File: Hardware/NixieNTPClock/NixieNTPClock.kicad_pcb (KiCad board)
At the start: 2 copper layers, 58 parts, among them J1 Conn_01x02_Male, Q1 BC850, Q2 Q_NMOS_GDS, Q3 FQT4N25TF, Q4 FQT4N25TF, Q5 FQT4N25TF, Q6 FQT4N25TF, U1 74HC7014, U10 DS18B20, U11 ESP32-nodeMCU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

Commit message: Continu on PCB ...
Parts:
- U3: footprint Housings_DIP:DIP-16_W7.62mm_Socket -> Package_DIP:DIP-16_W7.62mm_Socket_LongPads
- moved U10 193.5 mm to (238.8, 118.4), turned to 180 degrees
- moved C13 181.6 mm to (230.4, 118.6), turned to 90 degrees
- moved R14 158.8 mm to (234.2, 113.8), turned to 180 degrees
- moved C14 150.5 mm to (204.2, 107.7), turned to 90 degrees
- moved C15 137.0 mm to (198.1, 107.7), turned to 90 degrees
- moved U2 130.9 mm to (77.7, 87.1)
- moved Q4 118.9 mm to (140.7, 75.2), turned to 180 degrees
- moved Q1 109.1 mm to (87.1, 93.8), turned to 90 degrees
- moved RV1 107.9 mm to (90.7, 100.7)
- moved Q6 106.2 mm to (197.7, 75.2), turned to 180 degrees
- moved R16 106.0 mm to (205.2, 75.2), turned to 90 degrees
- moved C1 103.6 mm to (71.0, 97.3), turned to 180 degrees
- moved R2 94.5 mm to (87.1, 86.9), turned to 270 degrees
- moved R13 91.7 mm to (148.6, 75.2), turned to 90 degrees
- moved R15 87.2 mm to (156.2, 75.2), turned to 270 degrees
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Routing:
- net Net-(TP1-Pad1): track 0.00 -> 105.6 mm
- net Net-(R8-Pad1): track 0.00 -> 28.7 mm
- net Net-(U1-Pad2): track 0.00 -> 28.2 mm
- net GND: track 0.00 -> 27.9 mm
- net /5: track 112.0 -> 85.8 mm, vias 1 -> 0
- net +5V: track 0.00 -> 20.8 mm
- net TEMP: track 0.00 -> 20.8 mm
- net Net-(U1-Pad6): track 0.00 -> 17.8 mm
- net Net-(U1-Pad4): track 0.00 -> 17.7 mm
- net Net-(Q6-Pad2): track 0.00 -> 11.8 mm
- net Net-(Q3-Pad2): track 0.00 -> 11.8 mm
- net Net-(Q5-Pad2): track 0.00 -> 11.4 mm
- net Net-(Q4-Pad2): track 0.00 -> 11.3 mm
- net +3V3: track 0.00 -> 8.13 mm
- net P_UNIT_H: track 0.00 -> 4.84 mm
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
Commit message: Hardware: power supply
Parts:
- moved L2 121.4 mm to (106.0, 106.4)
- moved U9 116.3 mm to (99.1, 101.9), turned to 270 degrees
- moved R11 103.7 mm to (92.2, 111.3)
- moved C11 101.9 mm to (108.2, 115.3), turned to 270 degrees
- moved C9 93.9 mm to (92.4, 94.2), turned to 180 degrees
- moved C12 85.1 mm to (100.3, 115.3), turned to 270 degrees
- moved R10 85.0 mm to (92.2, 115.1), turned to 180 degrees
- moved L1 82.6 mm to (69.8, 55.1), turned to 90 degrees
- moved D1 79.0 mm to (80.3, 65.9), turned to 90 degrees
- moved R9 75.8 mm to (92.7, 102.6), turned to 90 degrees
- moved C10 71.8 mm to (100.3, 106.9), turned to 270 degrees
- moved R17 55.8 mm to (32.8, -2.79), turned to 180 degrees
- moved C6 52.4 mm to (91.2, 66.0)
- moved D2 45.8 mm to (31.2, 2.03)
- moved R7 44.8 mm to (90.5, 77.5)
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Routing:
- net +12V: track 0.00 -> 70.9 mm, vias 0 -> 2
- net +5V: track 20.8 -> 43.0 mm
- net Net-(R10-Pad2): track 0.00 -> 19.3 mm
- net Net-(C2-Pad1): track 0.00 -> 18.6 mm
- net Net-(C10-Pad2): track 0.00 -> 17.3 mm
- net Net-(C8-Pad1): track 0.00 -> 15.7 mm
- net Net-(D1-Pad2): track 0.00 -> 13.9 mm
- net Net-(R1-Pad2): track 0.00 -> 11.6 mm
- net Net-(R9-Pad1): track 0.00 -> 8.49 mm
- net Net-(Q2-Pad1): track 0.00 -> 6.15 mm
- net Net-(R6-Pad2): track 0.00 -> 4.12 mm
- net Net-(R7-Pad1): track 0.00 -> 3.98 mm
- net GND: track 27.9 -> 31.7 mm
- net Net-(C5-Pad2): track 0.00 -> 3.30 mm
- net Net-(C10-Pad1): track 0.00 -> 2.84 mm

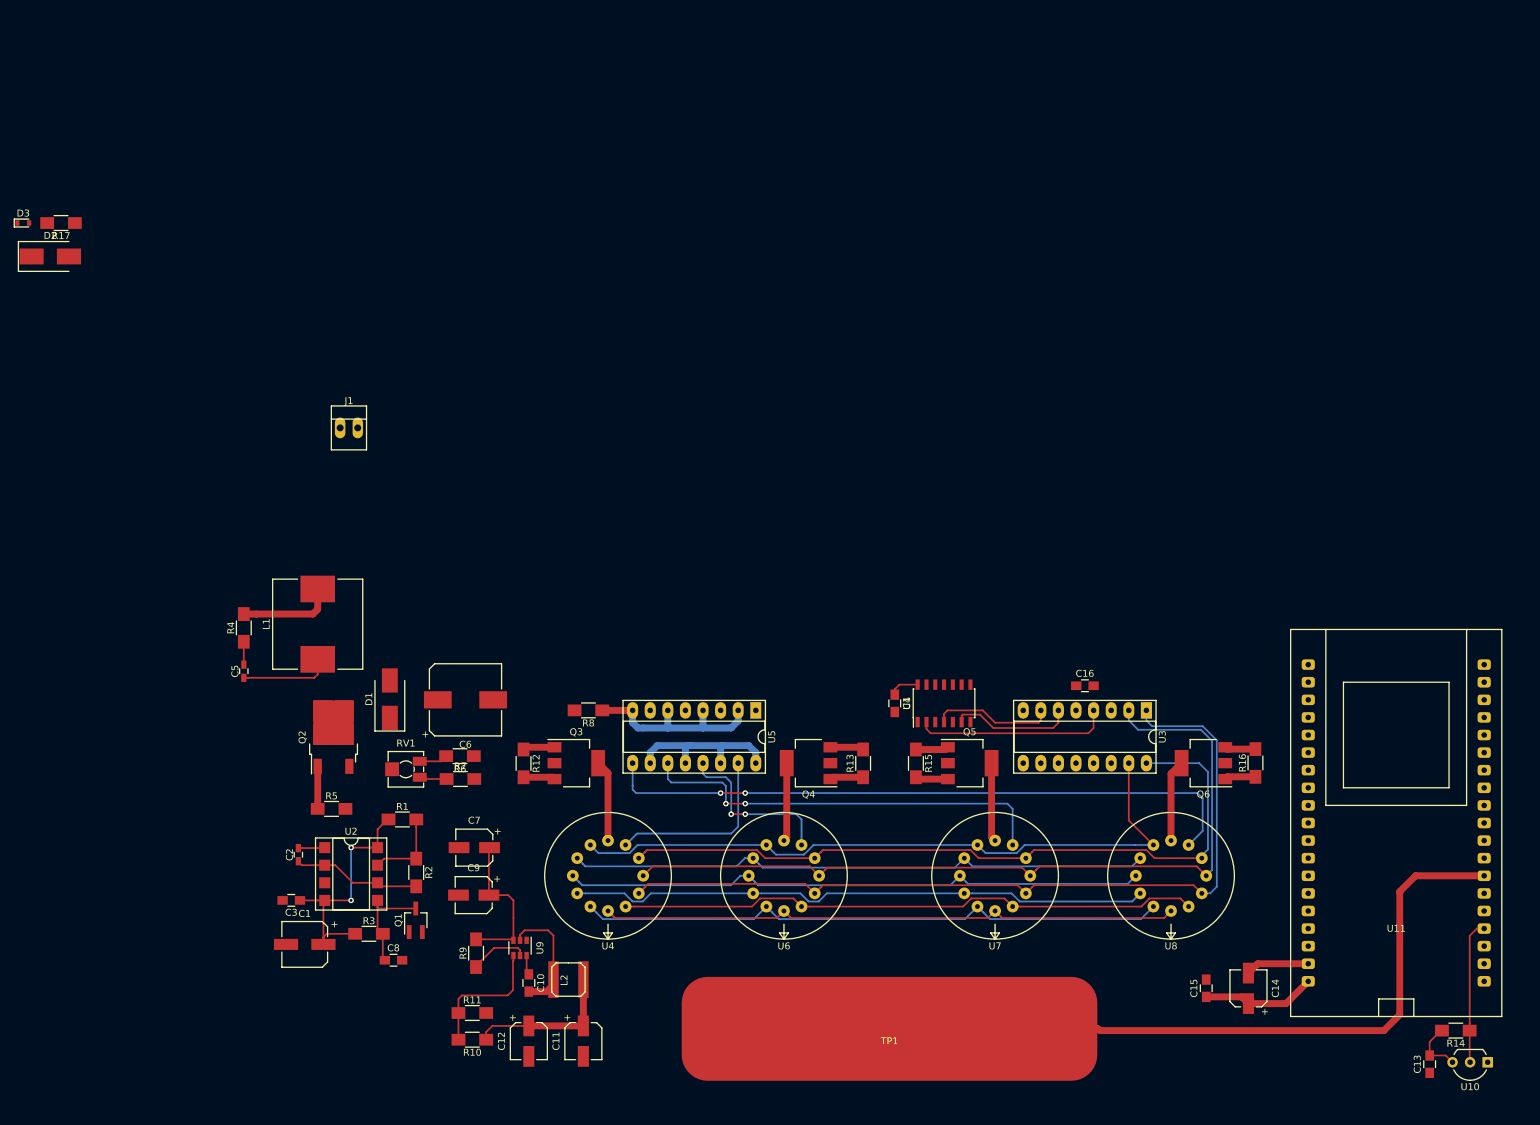
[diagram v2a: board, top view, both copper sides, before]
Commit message: Continuous routing ...
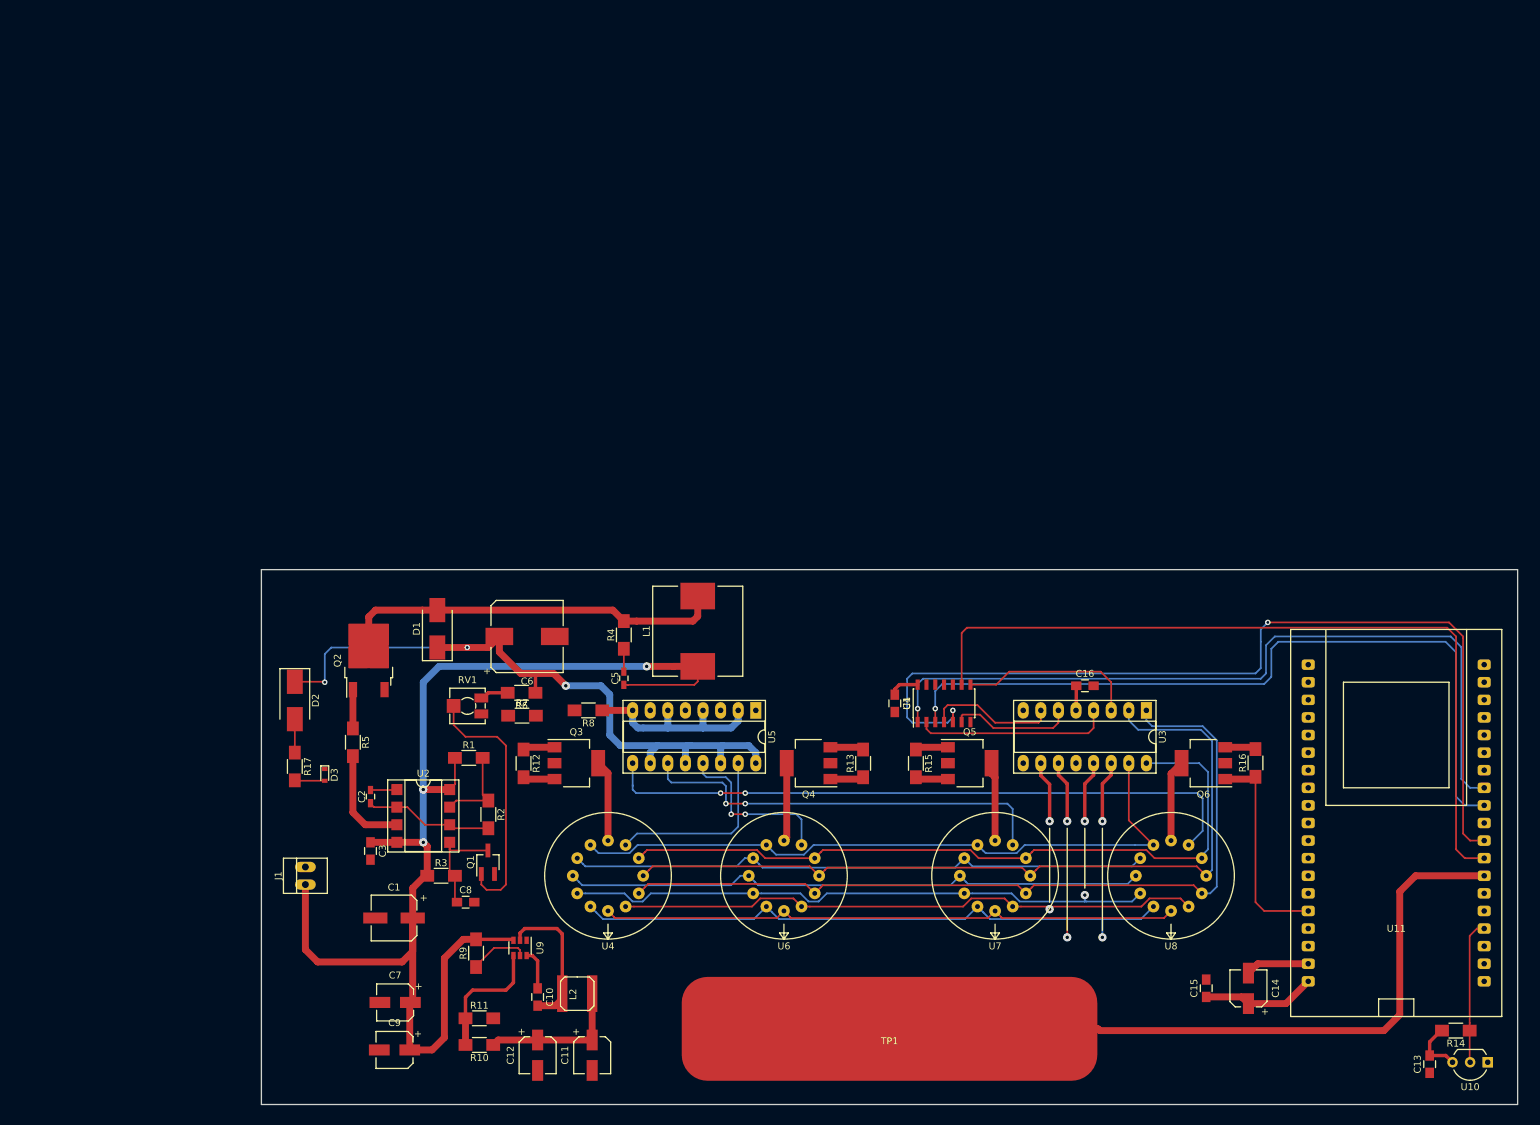
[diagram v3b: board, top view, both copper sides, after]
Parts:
- moved D3 90.8 mm to (70.9, 76.9), turned to 270 degrees
- moved R17 85.4 mm to (66.5, 75.7), turned to 270 degrees
- moved D2 73.2 mm to (66.5, 66.1), turned to 270 degrees
- moved J1 66.1 mm to (68.1, 92.7), turned to 90 degrees
- moved C5 54.9 mm to (114.0, 62.9)
- moved L1 54.9 mm to (124.7, 56.1)
- moved R4 54.9 mm to (114.0, 56.7)
- moved C9 25.1 mm to (80.9, 116.6)
- moved C7 25.1 mm to (81.0, 109.7)
- moved C3 13.5 mm to (77.5, 87.9), turned to 270 degrees
- moved C1 13.4 mm to (80.9, 97.5)
- moved C8 13.4 mm to (91.2, 95.2)
- moved R2 13.4 mm to (94.5, 82.6)
- moved R3 13.4 mm to (87.7, 91.4)
- moved U2 13.4 mm to (85.1, 82.8)
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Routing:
- net B: track 0.00 -> 135.2 mm, vias 0 -> 2
- net A: track 0.00 -> 115.0 mm
- net +12V: track 70.9 -> 183.9 mm, vias 2 -> 3
- net D: track 0.00 -> 112.7 mm, vias 0 -> 1
- net C: track 0.00 -> 111.0 mm, vias 0 -> 1
- net HV: track 24.9 -> 100.7 mm, vias 0 -> 3
- net Net-(D1-Pad2): track 13.9 -> 56.0 mm
- net Net-(Q1-Pad1): track 0.00 -> 37.3 mm
- net /6: track 83.8 -> 112.3 mm, vias 0 -> 2
- net /5: track 85.8 -> 114.1 mm, vias 0 -> 2
- net P_UNIT_M: track 4.51 -> 30.7 mm
- net Net-(U1-Pad8): track 0.00 -> 25.8 mm
- net /7: track 84.2 -> 106.3 mm, vias 0 -> 2
- net /4: track 84.2 -> 104.7 mm, vias 0 -> 2
- net Net-(R5-Pad2): track 0.00 -> 15.2 mm
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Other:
- board outline added: 181.4 x 77.2 mm
- copper layers 2 -> 4

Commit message: PCB almost finished
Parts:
- added REF**: MountingHole_5.3mm_M5_ISO7380_Pad, MountingHole:MountingHole_5.3mm_M5_ISO7380_Pad, F.Cu at (67.8, 118.4)
- added REF**: Symbol_Highvoltage_Type1_CopperTop_Small, Symbol:Symbol_Highvoltage_Type1_CopperTop_Small, F.Cu at (80.0, 72.4)
- added REF**: MountingHole_5.3mm_M5_ISO7380_Pad, MountingHole:MountingHole_5.3mm_M5_ISO7380_Pad, F.Cu at (67.8, 53.3)
- added REF**: MountingHole_5.3mm_M5_ISO7380_Pad, MountingHole:MountingHole_5.3mm_M5_ISO7380_Pad, F.Cu at (220.7, 118.4)
- added REF**: MountingHole_5.3mm_M5_ISO7380_Pad, MountingHole:MountingHole_5.3mm_M5_ISO7380_Pad, F.Cu at (225.3, 73.9)
- added REF**: OSHW-Symbol_6.7x6mm_SilkScreen, Symbol:OSHW-Symbol_6.7x6mm_SilkScreen, F.Cu at (188.0, 120.4)
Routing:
- net +5V: track 45.7 -> 240.4 mm, vias 0 -> 3
- net P_DIZ_H: track 4.61 -> 164.0 mm
- net P_UNIT_H: track 4.84 -> 133.0 mm, vias 0 -> 1
- net UNIT_M: track 0.00 -> 125.6 mm, vias 0 -> 1
- net P_DIZ_M: track 4.76 -> 123.8 mm, vias 0 -> 1
- net DIZ_M: track 0.00 -> 116.6 mm, vias 0 -> 1
- net UNIT_H: track 0.00 -> 109.0 mm, vias 0 -> 1
- net DIZ_H: track 0.00 -> 100.3 mm, vias 0 -> 1
- net +3V3: track 8.13 -> 78.6 mm, vias 0 -> 1
- net /2: track 84.4 -> 133.8 mm, vias 0 -> 3
- net GND: track 31.7 -> 78.9 mm, vias 0 -> 217
- net /3: track 84.5 -> 129.0 mm, vias 0 -> 2
- net Net-(U1-Pad8): track 25.8 -> 37.9 mm
- net Net-(R7-Pad1): track 0.00 -> 3.98 mm
- net A: track 115.0 -> 117.4 mm, vias 0 -> 2
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- added copper zone on B.Cu, net GND
- added copper zone on F.Cu, net GND
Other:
- board text added: "+12 VDC"
- board text added: "Alim +145V"
- board text added: "Alim +5V"
- board text added: "Horloge nixie NTP BOUCHARDON"
- board text added: "Tactile"
- board text added: "Température"

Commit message: Finished PCB and added pdf and gerber files
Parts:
- moved REF** 1.78 mm to (225.3, 75.7)
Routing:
- net +5V: track 240.4 -> 238.5 mm
- net HV: track 100.7 -> 99.4 mm
- net P_DIZ_M: track 123.8 -> 124.6 mm
- net Net-(U1-Pad6): track 17.8 -> 18.5 mm
- net Net-(C8-Pad1): track 15.7 -> 15.1 mm
- net GND: vias 217 -> 224
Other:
- board text added: "Bastian Bouchardon 2019 Cadeau du petit bonhomme"
